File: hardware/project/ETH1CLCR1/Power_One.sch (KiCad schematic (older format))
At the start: 16 parts, among them Q501 IRFR5410, U501 MAX5902, U502 TSR1-2450, U503 LM1117IMP-3.3/NOPB

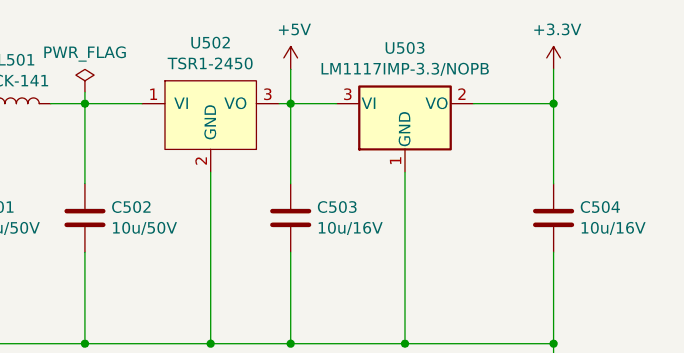
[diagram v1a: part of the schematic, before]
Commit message: Checked the schematics. Created BOM.
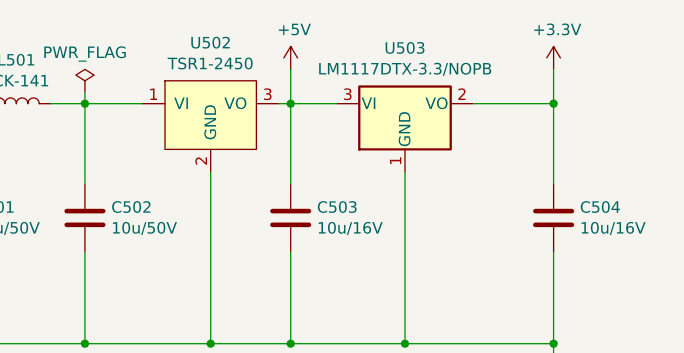
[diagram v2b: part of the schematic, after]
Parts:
- U503: value LM1117IMP-3.3/NOPB -> LM1117DTX-3.3/NOPB; footprint Package_TO_SOT_SMD:SOT-223-3_TabPin2 -> Package_TO_SOT_SMD:TO-252-2
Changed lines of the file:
@@
 P 8250 3250
 F 0 "U503" H 8250 3492 50  0000 C CNN
-F 1 "LM1117IMP-3.3/NOPB" H 8250 3401 50  0000 C CNN
-F 2 "Package_TO_SOT_SMD:SOT-223-3_TabPin2" H 8250 3250 50  0001 C CNN
+F 1 "LM1117DTX-3.3/NOPB" H 8250 3401 50  0000 C CNN
+F 2 "Package_TO_SOT_SMD:TO-252-2" H 8250 3250 50  0001 C CNN
 F 3 "http://www.ti.com/lit/ds/symlink/lm1117.pdf" H 8250 3250 50  0001 C CNN
 	1    8250 3250
